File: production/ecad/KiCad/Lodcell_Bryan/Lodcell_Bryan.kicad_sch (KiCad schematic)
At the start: 22 parts, among them J1 LoadCellConnector, J2 power_for_Loadcell, J3 ConnToESP32, U1 MIC920YC5-TR, U2 MIC920YC5-TR, U3 ADS1231IDR, U4 TXB0104DR

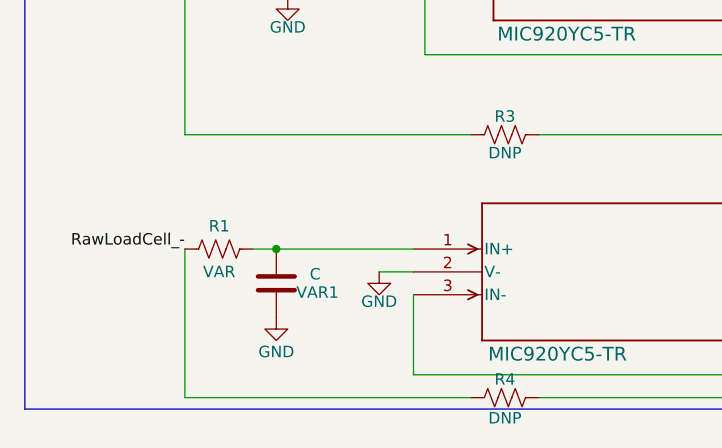
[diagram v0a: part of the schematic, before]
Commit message: Started layout
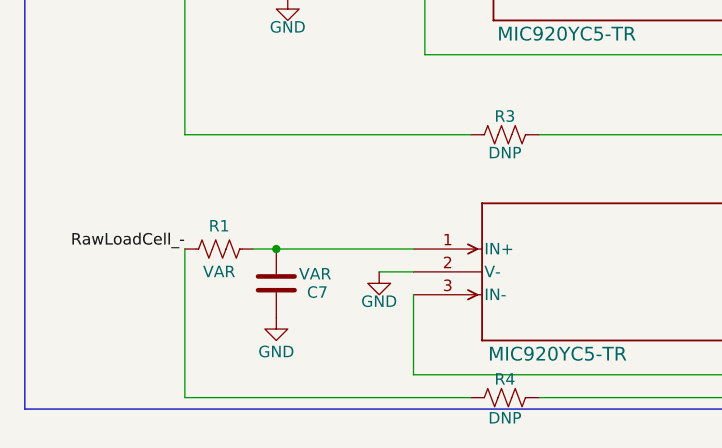
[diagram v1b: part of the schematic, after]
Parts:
- C7: renamed from VAR1; value C -> VAR
- J1: footprint BLT:JST_B2B-XH-A -> Connector_JST:JST_EH_B4B-EH-A_1x04_P2.50mm_Vertical
- J2: footprint (none) -> Connector_JST:JST_EH_B3B-EH-A_1x03_P2.50mm_Vertical
- J3: footprint (none) -> Connector_JST:JST_EH_B4B-EH-A_1x04_P2.50mm_Vertical
- TP1, TP2: footprint (none) -> TestPoint:TestPoint_2Pads_Pitch2.54mm_Drill0.8mm

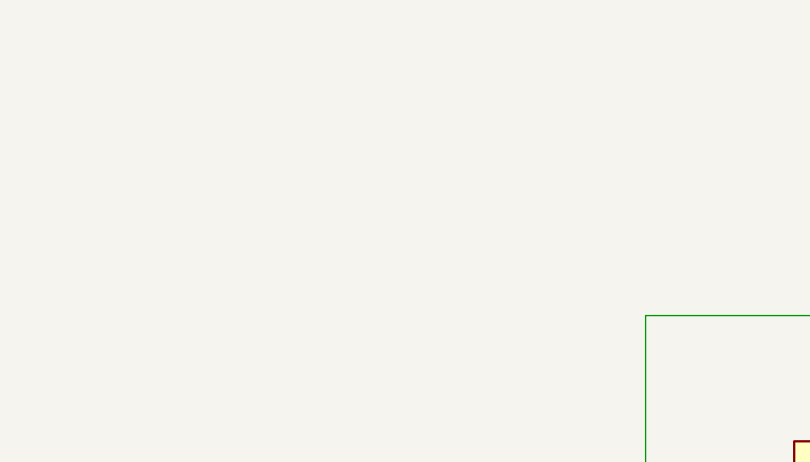
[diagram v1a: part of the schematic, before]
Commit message: Added mounting holes and very rough layout
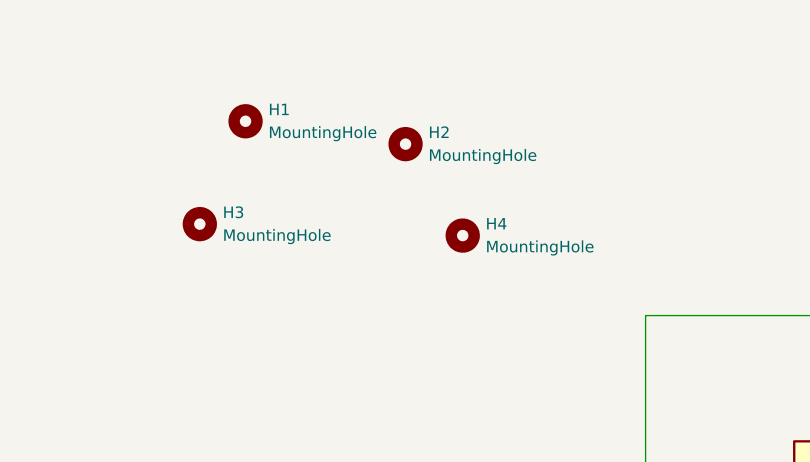
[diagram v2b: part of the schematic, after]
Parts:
- added H1, H2, H3, H4: MountingHole, MountingHole:MountingHole_2.5mm, symbol Mechanical:MountingHole

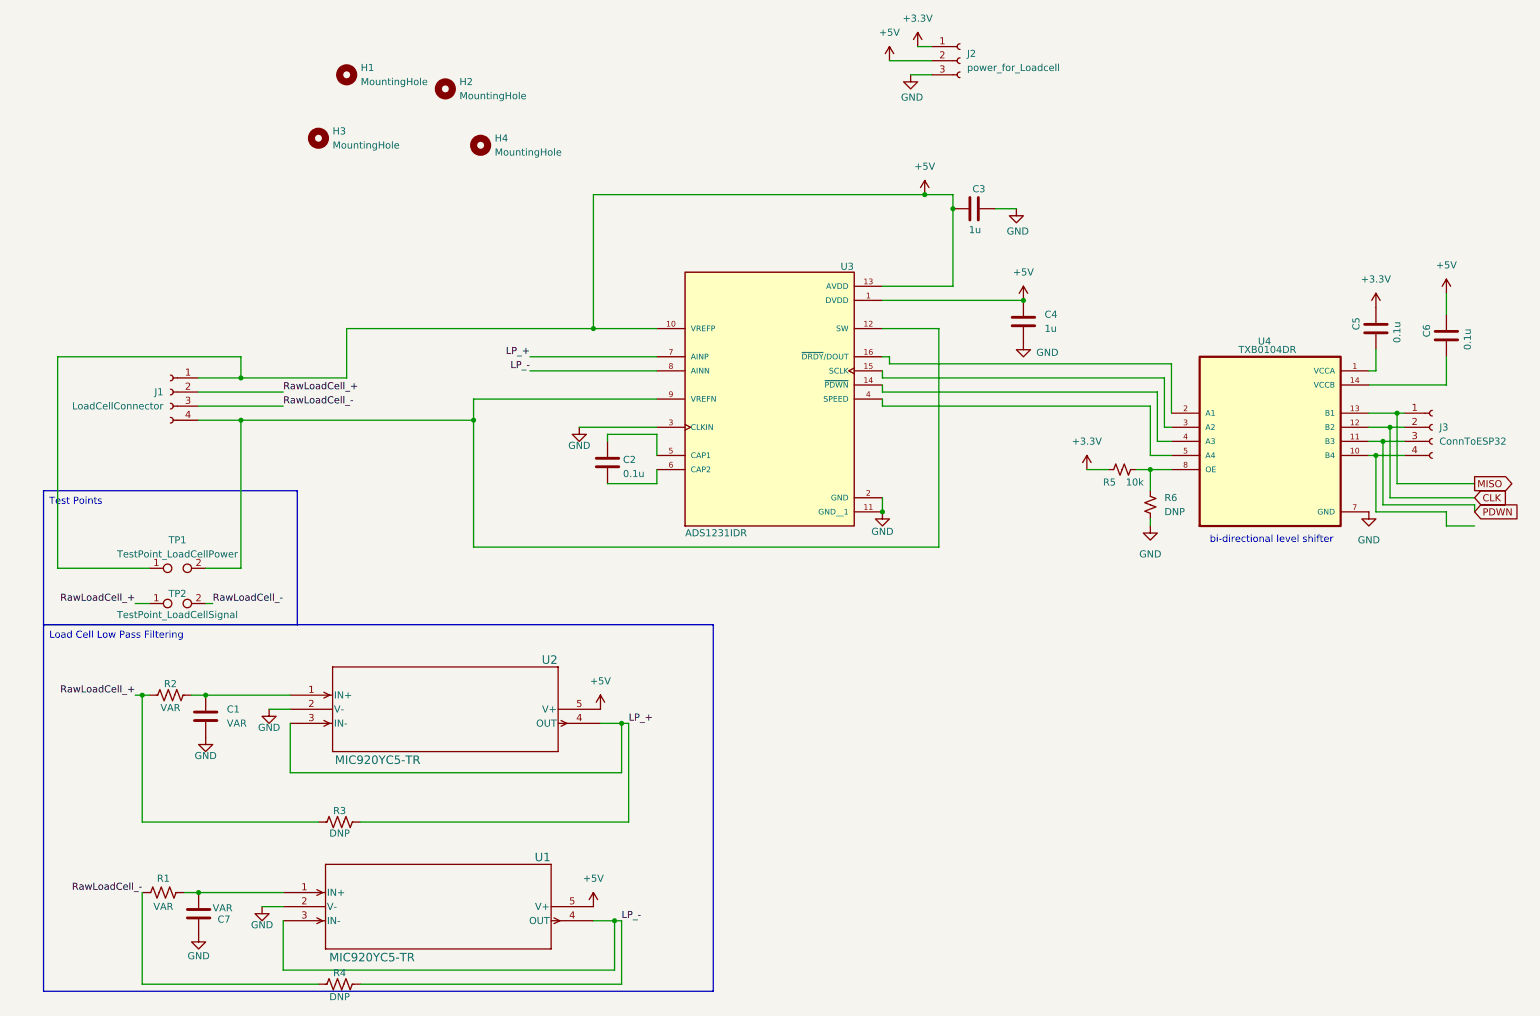
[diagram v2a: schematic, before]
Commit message: Load cell schematic changes
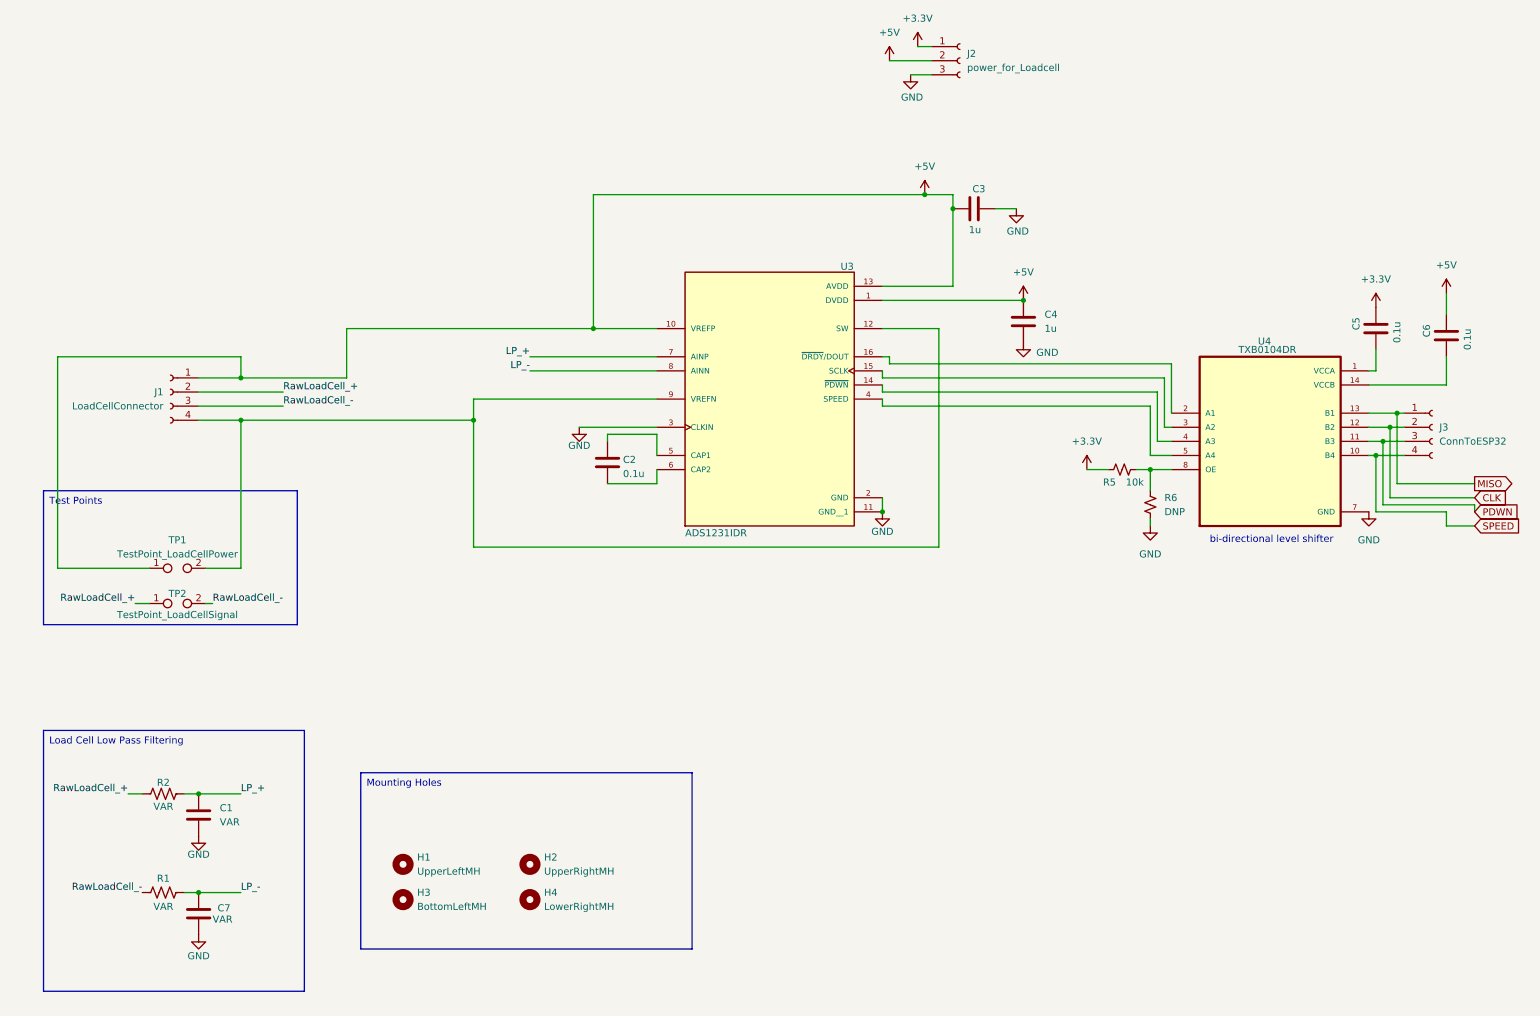
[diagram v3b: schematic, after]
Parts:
- removed R3, R4: DNP, Resistor_SMD:R_0805_2012Metric_Pad1.20x1.40mm_HandSolder, symbol Device:R_US
- removed U1, U2: MIC920YC5-TR, SC-70_C5_MCH, symbol 2024-10-08_01-43-59:MIC920YC5-TR
- H1: value MountingHole -> UpperLeftMH
- H2: value MountingHole -> UpperRightMH
- H3: value MountingHole -> BottomLeftMH
- H4: value MountingHole -> LowerRightMH
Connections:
- net GND: now also C7.1; no longer C7.2
- net LP_+: now also C1.1, R2.1
- net LP_-: now also C7.2, R1.1
- net SPEED: now reaches J3.4 (Pin_4), U4.10 (B4)
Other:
- moved on the sheet: C1, H1, H2, H3, H4, R2

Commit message: load cell footprint updates
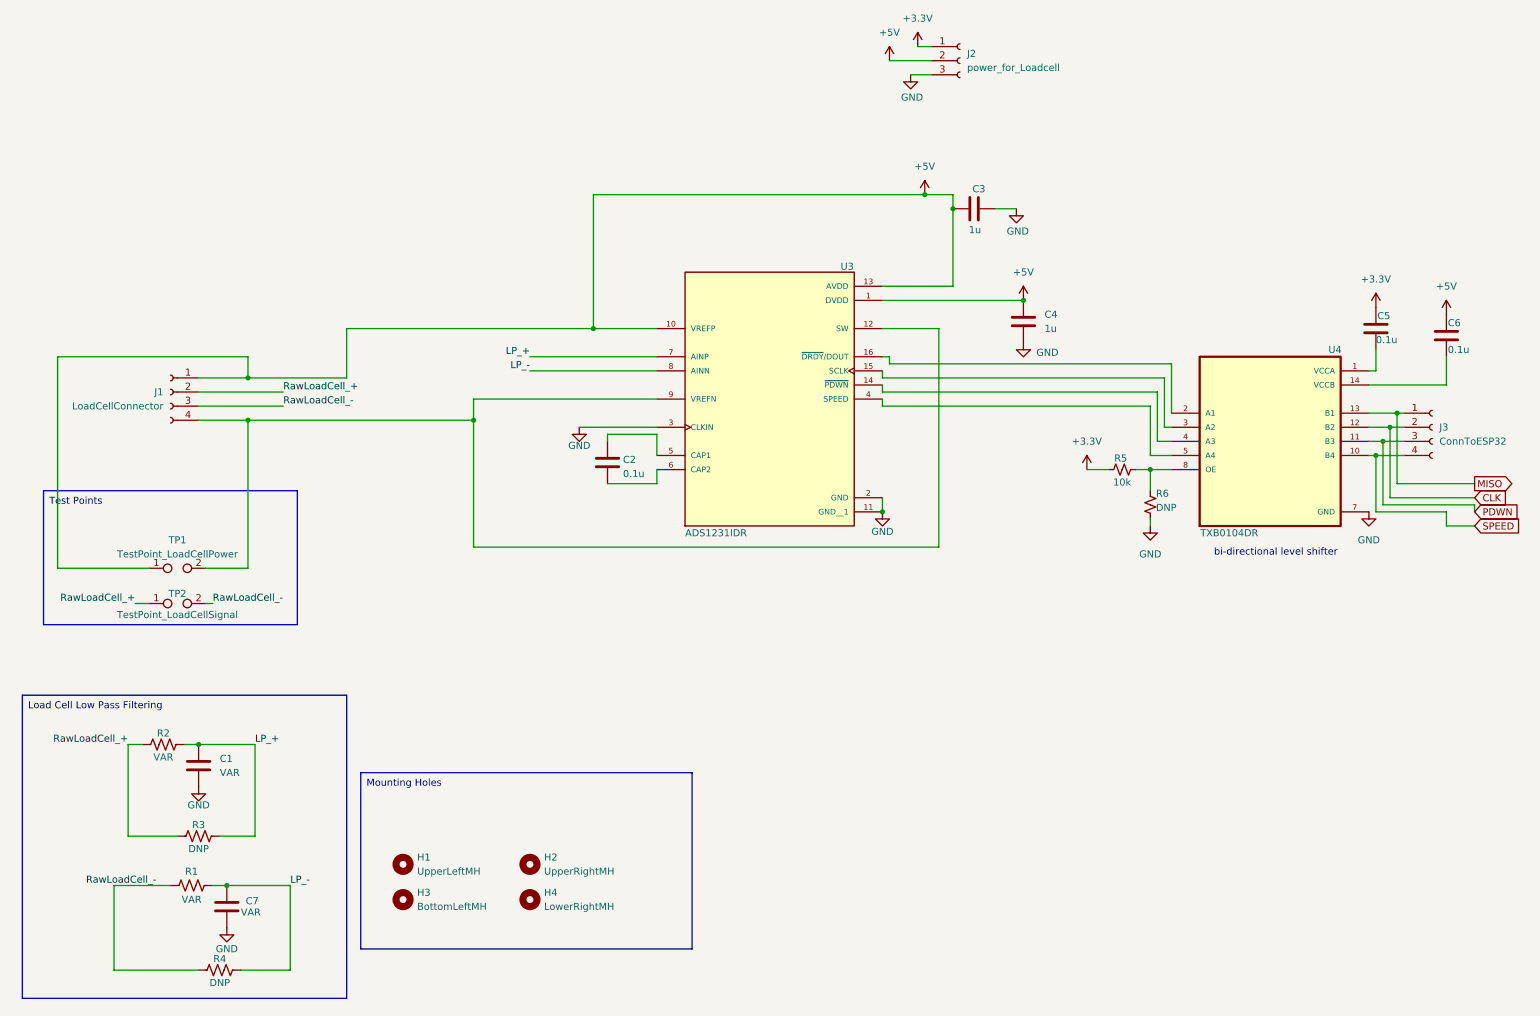
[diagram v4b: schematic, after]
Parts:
- added R3, R4: DNP, Resistor_SMD:R_0805_2012Metric_Pad1.20x1.40mm_HandSolder, symbol Device:R_US
- J1: footprint Connector_JST:JST_EH_B4B-EH-A_1x04_P2.50mm_Vertical -> CONN_B4B-XH-AM_JST:CONN_B4B-XH-AM_JST; Field5 (none) -> https://www.digikey.com/en/products/detail/jst-sales-americ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
- J3: footprint Connector_JST:JST_EH_B4B-EH-A_1x04_P2.50mm_Vertical -> CONN_B4B-XH-AM_JST:CONN_B4B-XH-AM_JST
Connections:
- net LP_+: now also R3.1
- net LP_-: now also R4.1
- net RawLoadCell_+: now also R3.2
- net RawLoadCell_-: now also R4.2
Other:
- moved on the sheet: C1, C7, R1, R2

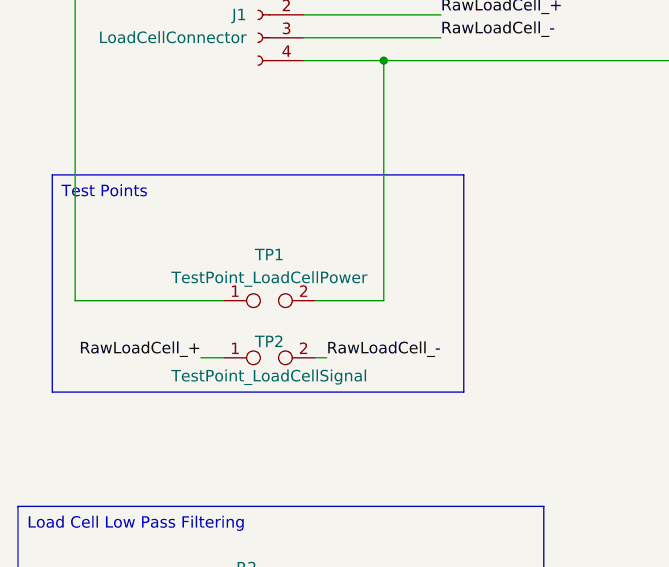
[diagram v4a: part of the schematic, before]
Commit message: deleted loadcell test point
no testpoint on diferential signal of loadcell
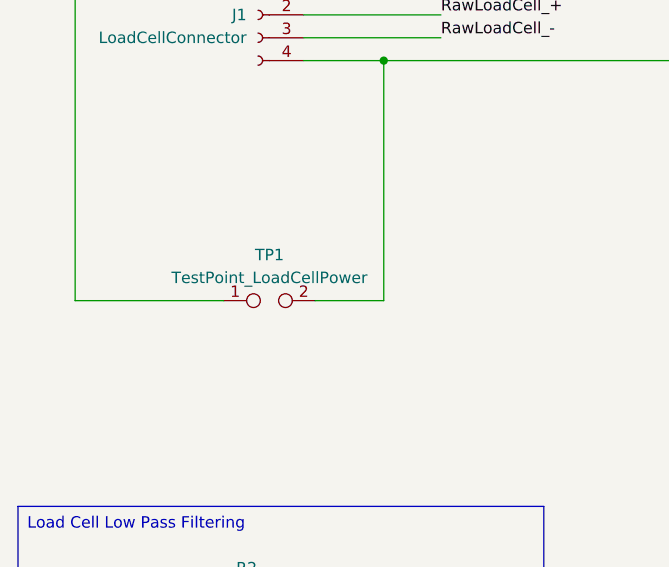
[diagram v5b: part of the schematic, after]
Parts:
- removed TP2: TestPoint_LoadCellSignal, TestPoint:TestPoint_2Pads_Pitch2.54mm_Drill0.8mm, symbol Connector:TestPoint_2Pole
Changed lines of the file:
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@@
-	(wire
-		(pts
-			(xy 48.26 125.73) (xy 46.99 125.73)
-		)
-		(stroke
-			(width 0)
-			(type default)
-		)
-	)
 	(wire
 		(pts
@@
 		(pts
 			(xy 217.17 90.17) (xy 168.91 90.17)
-		)
-		(stroke
-			(width 0)
-			(type default)
-		)
-	)
-	(wire
-		(pts
-			(xy 36.83 125.73) (xy 34.29 125.73)
 		)
 		(stroke
@@
 		)
 	)
-	(text_box "Test Points"
-		(exclude_from_sim no)
-		(at 17.78 105.41 0)
-		(size 45.72 24.13)
-		(stroke
-			(width 0)
-			(type default)
-		)
-		(fill
-			(type none)
-		)
-		(effects
-			(font
-				(size 1.27 1.27)
-			)
-			(justify left top)
-		)
-	)
 	(text "bi-directional level shifter"
 		(exclude_from_sim no)
@@
 		)
 	)
-	(label "RawLoadCell_+"
-		(at 34.29 125.73 180)
-		(fields_autoplaced yes)
-		(effects
-			(font
-				(size 1.27 1.27)
-			)
-			(justify right bottom)
-		)
-	)
 	(label "LP_+"
 		(at 105.41 81.28 180)
@@
 			)
 			(justify right bottom)
-		)
-	)
-	(label "RawLoadCell_-"
-		(at 48.26 125.73 0)
-		(fields_autoplaced yes)
-		(effects
-			(font
-				(size 1.27 1.27)
-			)
-			(justify left bottom)
 		)
 	)
@@
 					(unit 1)
 				)
-			)
-		)
-	)
-	(symbol
-		(lib_id "Connector:TestPoint_2Pole")
-		(at 41.91 125.73 0)
-		(unit 1)
-		(exclude_from_sim no)
-		(in_bom yes)
-		(on_board yes)
-		(dnp no)
-		(property "Reference" "TP2"
-			(at 41.91 123.952 0)
-			(effects
-				(font
-					(size 1.27 1.27)
-				)
-			)
-		)
-		(property "Value" "TestPoint_LoadCellSignal"
-			(at 41.91 127.762 0)
-			(effects
-				(font
-					(size 1.27 1.27)
-				)
-			)
-		)
-		(property "Footprint" "TestPoint:TestPoint_2Pads_Pitch2.54mm_Drill0.8mm"
-			(at 41.91 125.73 0)
-			(effects
-				(font
-					(size 1.27 1.27)
-				)
-				(hide yes)
-			)
-		)
-		(property "Datasheet" "~"
-			(at 41.91 125.73 0)
-			(effects
-				(font
-					(size 1.27 1.27)
-				)
-				(hide yes)
-			)
-		)
-		(property "Description" "2-polar test point"
-			(at 41.91 125.73 0)
-			(effects
-				(font
-					(size 1.27 1.27)
-				)
-				(hide yes)
-			)
-		)
-		(pin "2"
-		)
-		(pin "1"
-		)
-		(instances
-			(project "Lodcell_Bryan"
-				(path "/3f57d594-36f2-42e1-9017-f4e9011de5a2"
-					(reference "TP2")
-					(unit 1)
-				)

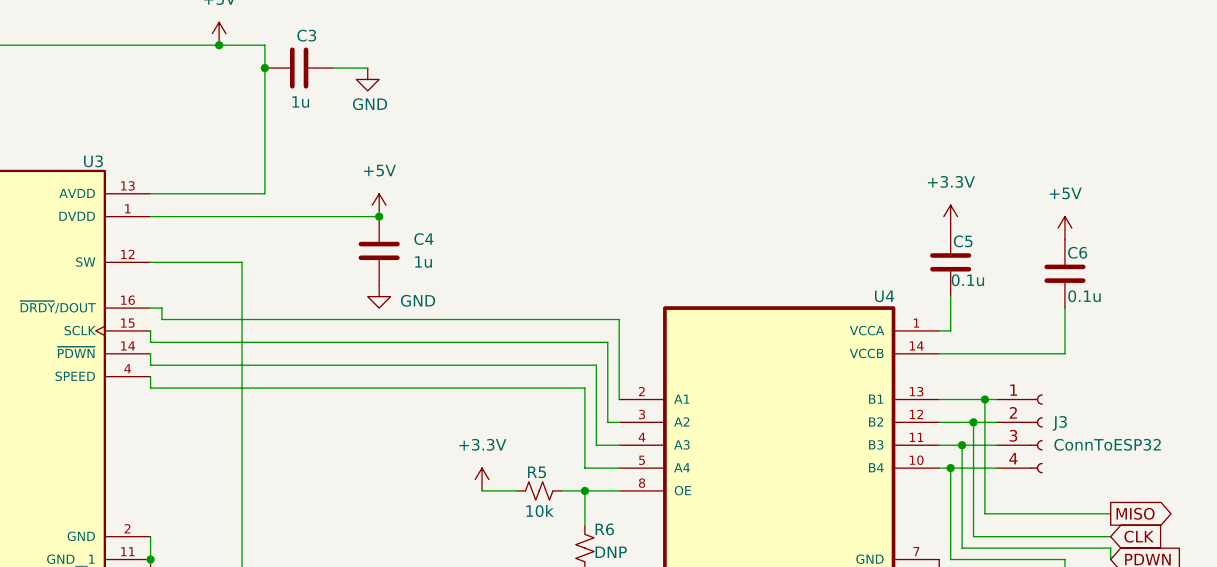
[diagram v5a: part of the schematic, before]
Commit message: Layout for loadcell
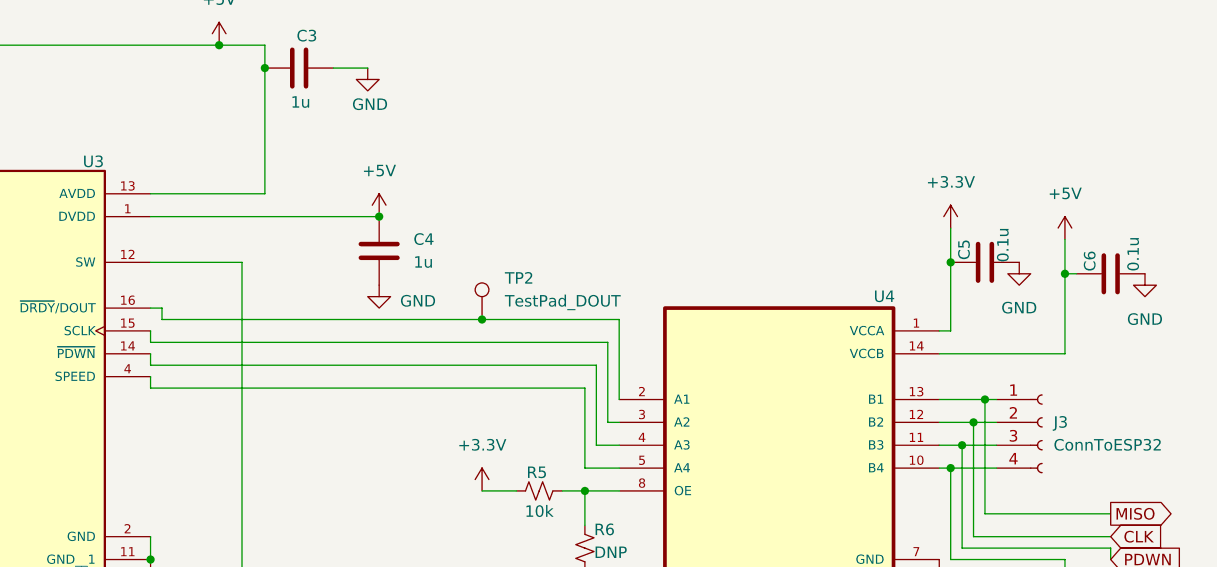
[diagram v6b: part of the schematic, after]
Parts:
- added TP2: TestPad_DOUT, symbol Connector:TestPoint
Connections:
- net +3.3V: now also U4.1 (VCCA)
- net +5V: now also U4.14 (VCCB)
- net GND: now also C5.1, C6.1
- net at U3.16 (~{DRDY}/DOUT), U4.2 (A1): now also TP2.1

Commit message: Added DOUT test point
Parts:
- TP2: footprint (none) -> TestPoint:TestPoint_Pad_D1.5mm
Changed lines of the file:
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@@
 			)
 		)
-		(property "Footprint" ""
+		(property "Footprint" "TestPoint:TestPoint_Pad_D1.5mm"
 			(at 210.82 82.55 0)
 			(effects
